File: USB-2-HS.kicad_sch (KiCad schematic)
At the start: 18 parts, among them J900 U-M-M5DW-W-1, U900 USB3320C-EZK-TR, X900 ECS-2520MV-130-BN

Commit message: all page
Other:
- title: (none) -> USB 2.0 High-Speed (OTG)
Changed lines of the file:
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@@
 	(generator_version "8.0")
 	(paper "A4")
+	(title_block
+		(title "USB 2.0 High-Speed (OTG)")
+		(date "2024-12-05")
+	)
 	(junction
 		(at 128.27 116.84)

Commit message: all page
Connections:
- net GND: now also J900.6, J900.7
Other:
- moved on the sheet: C6, C901, C902, C903, C904, C905, C906, D900, D901, D902, FB900, J900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

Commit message: sch-to-pcb
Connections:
- net USB_PHY_RBIAS: now reaches R902.2, U900.24 (RBIAS)
- net +5V_USB_AB: now reaches C906.1, FB900.2, J900.1 (VCC)
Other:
- moved on the sheet: R902
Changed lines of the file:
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@@
+	)
+	(junction
+		(at 242.57 63.5)
+		(diameter 0)
+		(color 0 0 0 0)
 	)
 	(junction
@@
 	(wire
 		(pts
-			(xy 156.21 109.22) (xy 165.1 109.22)
+			(xy 156.21 109.22) (xy 171.45 109.22)
 		)
 		(stroke
@@
 	(wire
 		(pts
-			(xy 220.98 63.5) (xy 247.65 63.5)
+			(xy 220.98 63.5) (xy 242.57 63.5)
 		)
 		(stroke
@@
 	(wire
 		(pts
+			(xy 242.57 62.23) (xy 242.57 63.5)
+		)
+		(stroke
+			(width 0)
+			(type default)
+		)
+	)
+	(wire
+		(pts
 			(xy 158.75 99.06) (xy 158.75 101.6)
 		)
@@
 	(wire
 		(pts
+			(xy 242.57 63.5) (xy 247.65 63.5)
+		)
+		(stroke
+			(width 0)
+			(type default)
+		)
+	)
+	(wire
+		(pts
 			(xy 156.21 68.58) (xy 182.88 68.58)
 		)
@@
 	(wire
 		(pts
-			(xy 165.1 109.22) (xy 165.1 110.49)
+			(xy 171.45 109.22) (xy 171.45 110.49)
 		)
 		(stroke
@@
 	(wire
 		(pts
-			(xy 158.75 118.11) (xy 165.1 118.11)
+			(xy 158.75 118.11) (xy 171.45 118.11)
 		)
 		(stroke
@@
 		)
 	)
+	(label "USB_PHY_RBIAS"
+		(at 171.45 109.22 180)
+		(fields_autoplaced yes)
+		(effects
+			(font
+				(size 0.762 0.762)
+			)
+			(justify right bottom)
+		)
+	)
 	(label "USB_HS_D_P"
 		(at 161.29 71.12 0)
@@
 			(font
 				(size 0.762 0.762)
-				(thickness 0.254)
-				(bold yes)
+				(thickness 0.0953)
 			)
 			(justify right)
@@
 			(font
 				(size 0.762 0.762)
-				(thickness 0.254)
-				(bold yes)
+				(thickness 0.0953)
 			)
 			(justify right)
@@
 			(font
 				(size 0.762 0.762)
-				(thickness 0.254)
-				(bold yes)
+				(thickness 0.0953)
 			)
 			(justify right)
@@
 			(font
 				(size 0.762 0.762)
-				(thickness 0.254)
-				(bold yes)
+				(thickness 0.0953)
 			)
 			(justify right)
@@
 			(font
 				(size 0.762 0.762)
-				(thickness 0.254)
-				(bold yes)
+				(thickness 0.0953)
 			)
 			(justify right)
@@
 			(font
 				(size 0.762 0.762)
-				(thickness 0.254)
-				(bold yes)
+				(thickness 0.0953)
 			)
 			(justify right)
@@
 			(font
 				(size 0.762 0.762)
-				(thickness 0.254)
-				(bold yes)
+				(thickness 0.0953)
 			)
 			(justify right)
@@
 			(font
 				(size 0.762 0.762)
-				(thickness 0.254)
-				(bold yes)
+				(thickness 0.0953)
 			)
 			(justify right)
@@
 			(font
 				(size 0.762 0.762)
-				(thickness 0.254)
-				(bold yes)
+				(thickness 0.0953)
 			)
 			(justify right)
@@
 			(font
 				(size 0.762 0.762)
-				(thickness 0.254)
-				(bold yes)
+				(thickness 0.0953)
 			)
 			(justify right)
@@
 			(font
 				(size 0.762 0.762)
+				(thickness 0.0953)
+			)
+			(justify right)
+		)
+		(property "Intersheetrefs" "${INTERSHEET_REFS}"
+			(at 81.6615 66.04 0)
+			(effects
+				(font
+					(size 1.27 1.27)
+				)
+				(justify right)
+				(hide yes)
+			)
+		)
+	)
+	(global_label "USB_NRST"
+		(shape input)
+		(at 69.85 99.06 180)
+		(fields_autoplaced yes)
+		(effects
+			(font
+				(size 0.762 0.762)
 				(thickness 0.254)
 				(bold yes)
@@
 		)
 		(property "Intersheetrefs" "${INTERSHEET_REFS}"
-			(at 81.6615 66.04 0)
+			(at 61.8494 99.06 0)
 			(effects
 				(font
@@
 			(font
 				(size 0.762 0.762)
-				(thickness 0.254)
-				(bold yes)
+				(thickness 0.0953)
 			)
 			(justify right)
@@
 	(symbol
 		(lib_id "Device:R")
-		(at 165.1 114.3 180)
+		(at 171.45 114.3 180)
 		(unit 1)
 		(exclude_from_sim no)
@@
 		(dnp no)
 		(property "Reference" "R902"
-			(at 168.91 113.03 0)
+			(at 175.26 113.03 0)
 			(effects
 				(font
@@
 		)
 		(property "Value" "8K06"
-			(at 169.418 114.554 0)
+			(at 175.768 114.554 0)
 			(effects
 				(font
@@
 		)
 		(property "Footprint" "Resistor_SMD:R_0402_1005Metric"
-			(at 166.878 114.3 90)
+			(at 173.228 114.3 90)
 			(effects
 				(font
@@
 		)
 		(property "Datasheet" "~"
-			(at 165.1 114.3 0)
+			(at 171.45 114.3 0)
 			(effects
 				(font
@@
 		)
 		(property "Description" "Resistor"
-			(at 165.1 114.3 0)
+			(at 171.45 114.3 0)
 			(effects
 				(font
@@
 		)
 		(property "LCSC" "C25923"
-			(at 165.1 114.3 0)
+			(at 171.45 114.3 0)
 			(effects
 				(font
@@
 		)
 		(property "Manufacturer Part Number" "0402WGF8061TCE"
-			(at 165.1 114.3 0)
+			(at 171.45 114.3 0)
 			(effects
 				(font
@@
 		(on_board yes)
 		(dnp no)
-		(fields_autoplaced yes)
 		(property "Reference" "J900"
-			(at 260.35 52.07 0)
+			(at 260.35 56.134 0)
 			(effects
 				(font
@@
 		)
 		(property "Value" "U-M-M5DW-W-1"
-			(at 260.35 55.88 0)
-			(effects
-				(font
-					(size 1.8288 1.8288)
+			(at 260.858 88.9 0)
+			(effects
+				(font
+					(size 1.27 1.27)
 				)
 			)
@@
 					(unit 1)
 				)
+			)
+		)
+	)
+	(symbol
+		(lib_id "power:+5V")
+		(at 242.57 62.23 0)
+		(unit 1)
+		(exclude_from_sim no)
+		(in_bom yes)
+		(on_board yes)
+		(dnp no)
+		(property "Reference" "#PWR051"
+			(at 242.57 66.04 0)
+			(effects
+				(font
+					(size 1.27 1.27)
+				)
+				(hide yes)
+			)
+		)
+		(property "Value" "+5V_USB_AB"
+			(at 242.316 58.674 0)
+			(effects
+				(font
+					(size 1.27 1.27)
+				)
+			)
+		)
+		(property "Footprint" ""
+			(at 242.57 62.23 0)
+			(effects
+				(font
+					(size 1.27 1.27)
+				)
+				(hide yes)
+			)
+		)
+		(property "Datasheet" ""
+			(at 242.57 62.23 0)
+			(effects
+				(font
+					(size 1.27 1.27)
+				)
+				(hide yes)
+			)
+		)
+		(property "Description" "Power symbol creates a global label with name \"+5V\""
+			(at 242.57 62.23 0)
+			(effects
+				(font
+					(size 1.27 1.27)
+				)
+				(hide yes)
+			)
+		)
+		(pin "1"
+		)
+		(instances
+			(project ""
+				(path "/068a81e1-1783-4521-9958-788ddeed3b49/9a41251a-1e05-4c4b-8495-bdec66c692fb"
+					(reference "#PWR051")
+					(unit 1)
+				)

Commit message: ram-update
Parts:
- FB900: footprint FB_0402 -> Footprint-Lib-PhilsLab:FB_0402
- U900: footprint QFN-32-5x5x0.85mm -> Footprint-Lib-PhilsLab:QFN-32-5x5x0.85mm
- X900: footprint XTAL_2520 -> Footprint-Lib-PhilsLab:XTAL_2520
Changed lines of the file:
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@@
 			)
 		)
-		(property "Footprint" "QFN-32-5x5x0.85mm"
+		(property "Footprint" "Footprint-Lib-PhilsLab:QFN-32-5x5x0.85mm"
 			(at 128.27 86.36 0)
 			(effects
@@
 			)
 		)
-		(property "Footprint" "FB_0402"
+		(property "Footprint" "Footprint-Lib-PhilsLab:FB_0402"
 			(at 212.09 63.5 0)
 			(effects
@@
 			)
 		)
-		(property "Footprint" "XTAL_2520"
+		(property "Footprint" "Footprint-Lib-PhilsLab:XTAL_2520"
 			(at 43.18 104.14 0)
 			(effects

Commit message: ram-zynq-updated
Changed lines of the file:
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@@
+	(wire
+		(pts
+			(xy 153.67 46.99) (xy 153.67 44.45)
+		)
+		(stroke
+			(width 0)
+			(type default)
+		)
+	)
 	(wire
 		(pts
@@
 		(pts
 			(xy 158.75 101.6) (xy 156.21 101.6)
+		)
+		(stroke
+			(width 0)
+			(type default)
+		)
+	)
+	(wire
+		(pts
+			(xy 153.67 34.29) (xy 153.67 36.83)
 		)
 		(stroke
@@
 	(symbol
 		(lib_id "power:+1V0")
-		(at 153.67 36.83 0)
+		(at 153.67 34.29 0)
 		(unit 1)
 		(exclude_from_sim no)
@@
 		(fields_autoplaced yes)
 		(property "Reference" "#PWR0198"
-			(at 153.67 40.64 0)
+			(at 153.67 38.1 0)
 			(effects
 				(font
@@
 		)
 		(property "Value" "+1V8"
-			(at 153.67 31.75 0)
+			(at 153.67 29.21 0)
 			(effects
 				(font
@@
 		)
 		(property "Footprint" ""
-			(at 153.67 36.83 0)
+			(at 153.67 34.29 0)
 			(effects
 				(font
@@
 		)
 		(property "Datasheet" ""
-			(at 153.67 36.83 0)
+			(at 153.67 34.29 0)
 			(effects
 				(font
@@
 		)
 		(property "Description" "Power symbol creates a global label with name \"+1V0\""
-			(at 153.67 36.83 0)
+			(at 153.67 34.29 0)
 			(effects
 				(font
@@
 	(symbol
 		(lib_id "power:GND")
-		(at 153.67 44.45 0)
+		(at 153.67 46.99 0)
 		(unit 1)
 		(exclude_from_sim no)
@@
 		(dnp no)
 		(property "Reference" "#PWR0195"
-			(at 153.67 50.8 0)
+			(at 153.67 53.34 0)
 			(effects
 				(font
@@
 		)
 		(property "Value" "GND"
-			(at 151.638 47.752 0)
+			(at 151.638 50.292 0)
 			(effects
 				(font
@@
 		)
 		(property "Footprint" ""
-			(at 153.67 44.45 0)
+			(at 153.67 46.99 0)
 			(effects
 				(font
@@
 		)
 		(property "Datasheet" ""
-			(at 153.67 44.45 0)
+			(at 153.67 46.99 0)
 			(effects
 				(font
@@
 		)
 		(property "Description" "Power symbol creates a global label with name \"GND\" , ground"
-			(at 153.67 44.45 0)
-			(effects
-				(font
+			(at 153.67 46.99 0)
+			(effects
+				(font

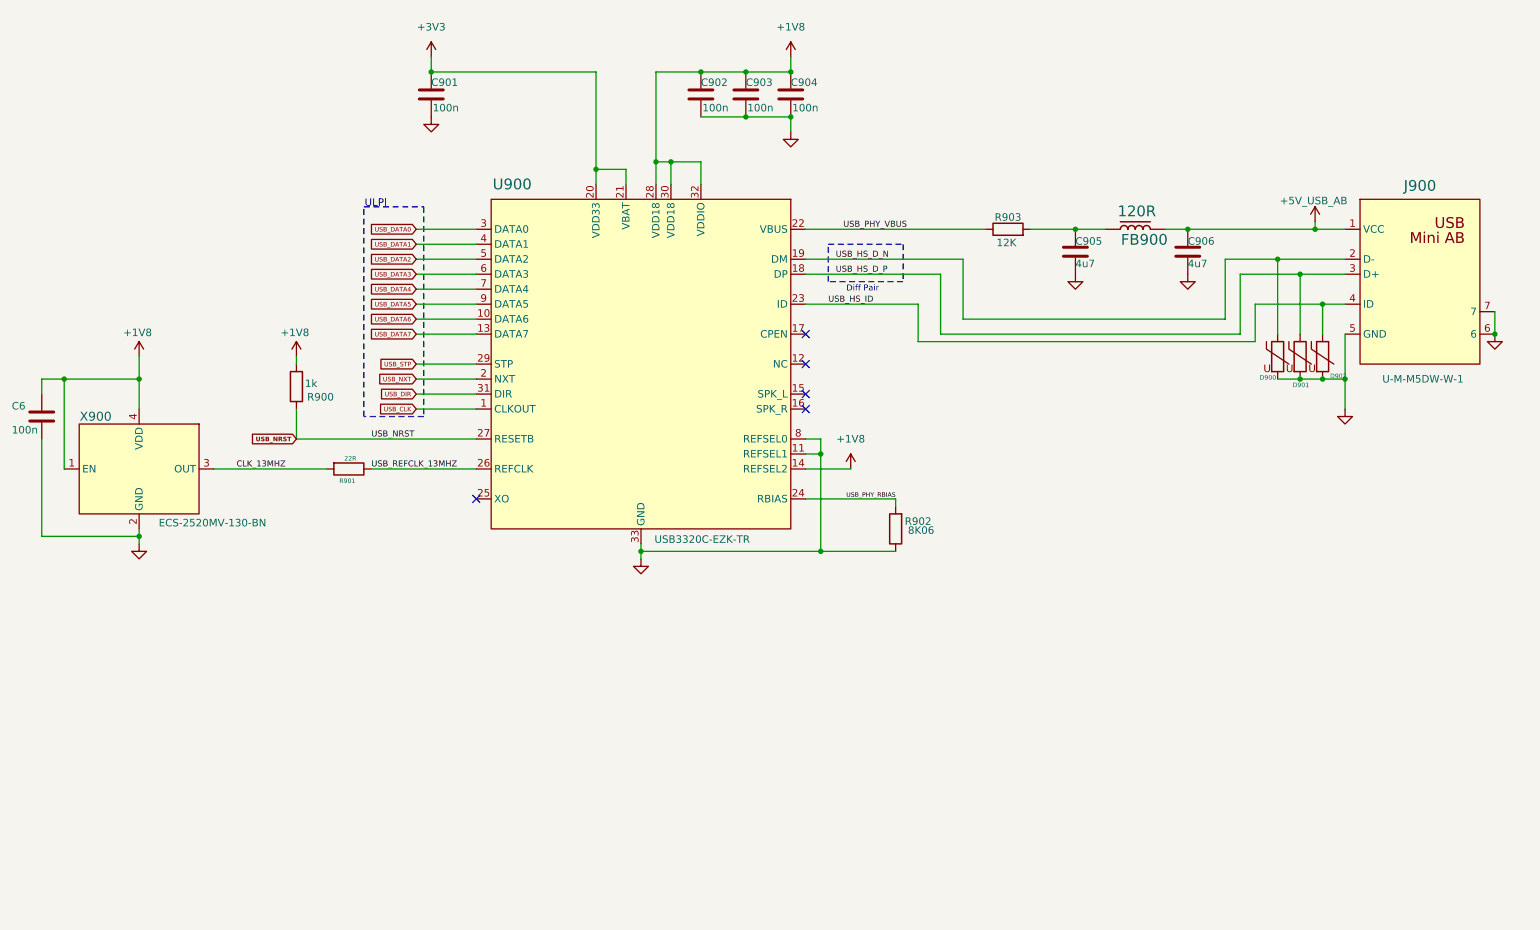
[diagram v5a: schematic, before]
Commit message: usb hs update
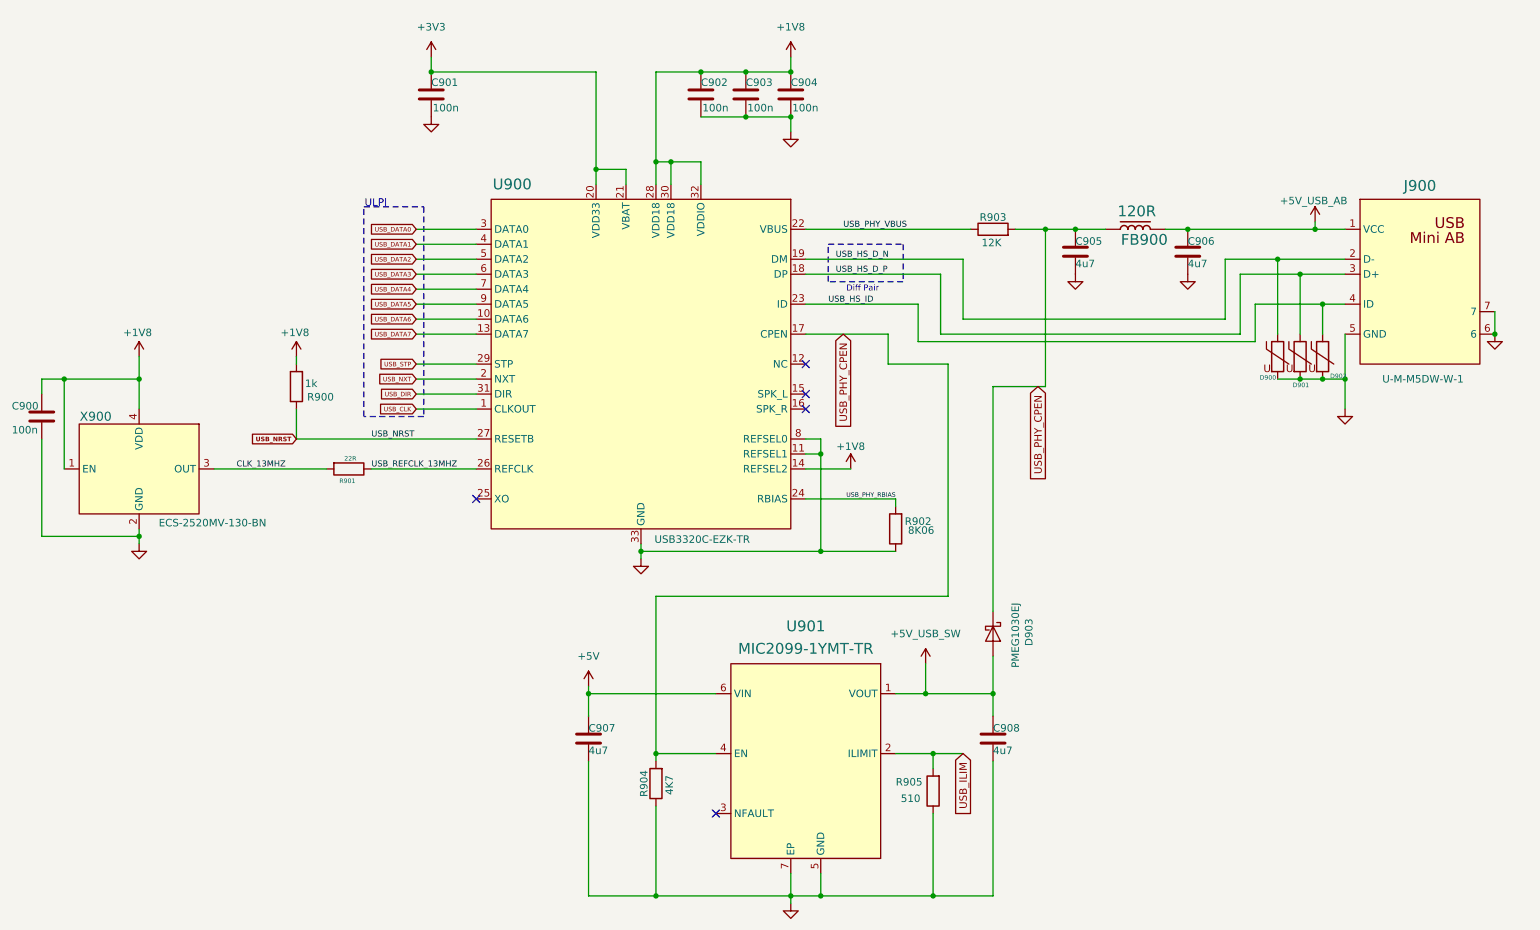
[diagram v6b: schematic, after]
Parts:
- added C907, C908: 4u7, Capacitor_SMD:C_0402_1005Metric, symbol Device:C
- added D903: PMEG1030EJ, Diode_SMD:D_SOD-323F, symbol Diode:PMEG1030EJ
- added R904: 4K7, Resistor_SMD:R_0402_1005Metric, symbol Device:R
- added R905: 510, Resistor_SMD:R_0402_1005Metric, symbol Device:R
- added U901: MIC2099-1YMT-TR, TMLF-6-1_6X1_6, symbol Schematic-Lib-PhilsLab:MIC2099-1YMT-TR
- renumbered C6 to C900
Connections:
- net GND: now also C907.2, C908.2, R904.1, R905.1, U901.5 (GND), U901.7 (EP)
- net USB_PHY_CPEN: now reaches C905.1, FB900.1, R903.2
- net USB_PHY_CPEN: now also U900.17 (CPEN), D903.1 (K), R904.2, U901.4 (EN)
- new net +5V: C907.1, U901.6 (VIN)
- new net +5V_USB_SW: C908.1, D903.2 (A), U901.1 (VOUT)
- new net USB_ILIM: R905.2, U901.2 (ILIMIT)
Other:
- moved on the sheet: R903

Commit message: pcb layers
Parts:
- D903: footprint Diode_SMD:D_SOD-323F -> easyeda2kicad_foorprint:SOD-323_L1.8-W1.3-LS2.5-RD
- U900: footprint Footprint-Lib-PhilsLab:QFN-32-5x5x0.85mm -> easyeda2kicad_foorprint:QFN-32_L5.0-W5.0-P0.50-BL-EP3.4
- U901: footprint TMLF-6-1_6X1_6 -> easyeda2kicad_foorprint:UDFN-6_L1.6-W1.6-P0.50-BL-EP1.2; LCSC (none) -> C621527
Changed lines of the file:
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@@
 			)
 		)
-		(property "Footprint" "Diode_SMD:D_SOD-323F"
+		(property "Footprint" "easyeda2kicad_foorprint:SOD-323_L1.8-W1.3-LS2.5-RD"
 			(at 183.515 132.08 0)
 			(effects
@@
 			)
 		)
-		(property "Footprint" "Footprint-Lib-PhilsLab:QFN-32-5x5x0.85mm"
+		(property "Footprint" "easyeda2kicad_foorprint:QFN-32_L5.0-W5.0-P0.50-BL-EP3.4"
 			(at 128.27 86.36 0)
 			(effects
@@
 			)
 		)
-		(property "Footprint" "TMLF-6-1_6X1_6"
+		(property "Footprint" "easyeda2kicad_foorprint:UDFN-6_L1.6-W1.6-P0.50-BL-EP1.2"
 			(at 156.21 154.94 0)
 			(effects
@@
 				(hide yes)
 			)
+		)
+		(property "LCSC" "C621527"
+			(at 156.21 154.94 0)
+			(effects
+				(font
+					(size 1.27 1.27)
+				)
+				(hide yes)
+			)

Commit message: pcbb
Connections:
- net GND: no longer J900.6, J900.7
- new net CGND: J900.6, J900.7
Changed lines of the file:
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@@
+	)
+	(junction
+		(at 146.05 36.83)
+		(diameter 0)
+		(color 0 0 0 0)
+	)
+	(junction
+		(at 176.53 142.24)
+		(diameter 0)
+		(color 0 0 0 0)
+	)
+	(junction
+		(at 30.48 88.9)
+		(diameter 0)
+		(color 0 0 0 0)
 	)
 	(junction
@@
 		(color 0 0 0 0)
 	)
-	(junction
-		(at 146.05 36.83)
-		(diameter 0)
-		(color 0 0 0 0)
-	)
-	(junction
-		(at 176.53 142.24)
-		(diameter 0)
-		(color 0 0 0 0)
-	)
-	(junction
-		(at 30.48 88.9)
-		(diameter 0)
-		(color 0 0 0 0)
-	)
 	(no_connect
 		(at 156.21 93.98)
@@
 		(pts
 			(xy 43.18 85.09) (xy 43.18 88.9)
+		)
+		(stroke
+			(width 0)
+			(type default)
+		)
+	)
+	(wire
+		(pts
+			(xy 275.59 81.28) (xy 273.05 81.28)
 		)
 		(stroke
@@
 				(path "/068a81e1-1783-4521-9958-788ddeed3b49/9a41251a-1e05-4c4b-8495-bdec66c692fb"
 					(reference "R904")
-					(unit 1)
-				)
-			)
-		)
-	)
-	(symbol
-		(lib_id "power:GND")
-		(at 273.05 81.28 0)
-		(unit 1)
-		(exclude_from_sim no)
-		(in_bom yes)
-		(on_board yes)
-		(dnp no)
-		(property "Reference" "#PWR050"
-			(at 273.05 87.63 0)
-			(effects
-				(font
-					(size 1.27 1.27)
-				)
-				(hide yes)
-			)
-		)
-		(property "Value" "GND"
-			(at 271.018 84.582 0)
-			(effects
-				(font
-					(size 1.27 1.27)
-				)
-				(hide yes)
-			)
-		)
-		(property "Footprint" ""
-			(at 273.05 81.28 0)
-			(effects
-				(font
-					(size 1.27 1.27)
-				)
-				(hide yes)
-			)
-		)
-		(property "Datasheet" ""
-			(at 273.05 81.28 0)
-			(effects
-				(font
-					(size 1.27 1.27)
-				)
-				(hide yes)
-			)
-		)
-		(property "Description" "Power symbol creates a global label with name \"GND\" , ground"
-			(at 273.05 81.28 0)
-			(effects
-				(font
-					(size 1.27 1.27)
-				)
-				(hide yes)
-			)
-		)
-		(pin "1"
-		)
-		(instances
-			(project "zynq_soc_board_v1"
-				(path "/068a81e1-1783-4521-9958-788ddeed3b49/9a41251a-1e05-4c4b-8495-bdec66c692fb"
-					(reference "#PWR050")
 					(unit 1)
 				)
@@
 					(unit 1)
 				)
+			)
+		)
+	)
+	(symbol
+		(lib_id "power:Earth")
+		(at 275.59 81.28 0)
+		(unit 1)
+		(exclude_from_sim no)
+		(in_bom yes)
+		(on_board yes)
+		(dnp no)
+		(property "Reference" "#PWR050"
+			(at 275.59 87.63 0)
+			(effects
+				(font
+					(size 1.27 1.27)
+				)
+				(hide yes)
+			)
+		)
+		(property "Value" "CGND"
+			(at 275.59 85.344 0)
+			(effects
+				(font
+					(size 1.27 1.27)
+				)
+			)
+		)
+		(property "Footprint" ""
+			(at 275.59 81.28 0)
+			(effects
+				(font
+					(size 1.27 1.27)
+				)
+				(hide yes)
+			)
+		)
+		(property "Datasheet" "~"
+			(at 275.59 81.28 0)
+			(effects
+				(font
+					(size 1.27 1.27)
+				)
+				(hide yes)
+			)
+		)
+		(property "Description" "Power symbol creates a global label with name \"Earth\""
+			(at 275.59 81.28 0)
+			(effects
+				(font
+					(size 1.27 1.27)
+				)
+				(hide yes)
+			)
+		)
+		(pin "1"
+		)
+		(instances
+			(project "zynq_soc_board_v1"
+				(path "/068a81e1-1783-4521-9958-788ddeed3b49/9a41251a-1e05-4c4b-8495-bdec66c692fb"
+					(reference "#PWR050")
+					(unit 1)
+				)
